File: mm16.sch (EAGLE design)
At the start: 58 parts, among them IC101 ATMEGA32-PU, IC102 DS1337, IC103 MAX483CPA, IC201 LTV847, IC202 LTV847, IC203 LTV847, IC204 LTV847, Q1 32,768kHz

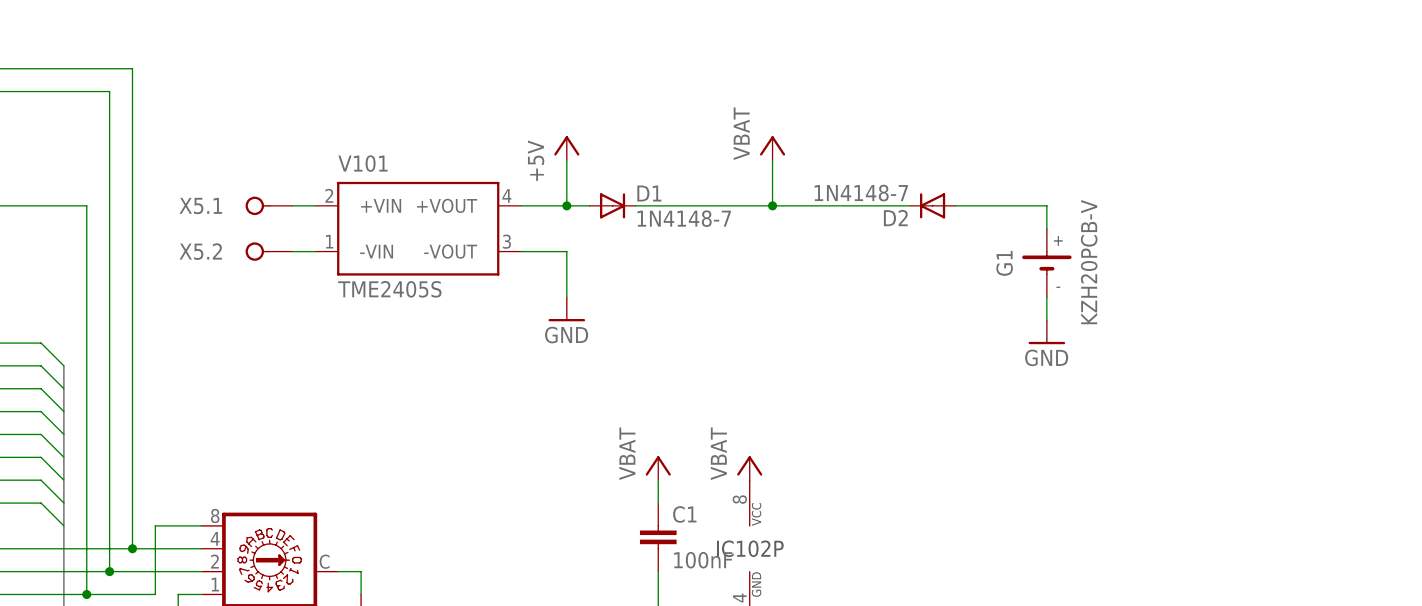
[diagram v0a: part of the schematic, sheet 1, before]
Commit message: Sicherheit und LED für Spannungsversorgung hinzugefuegt
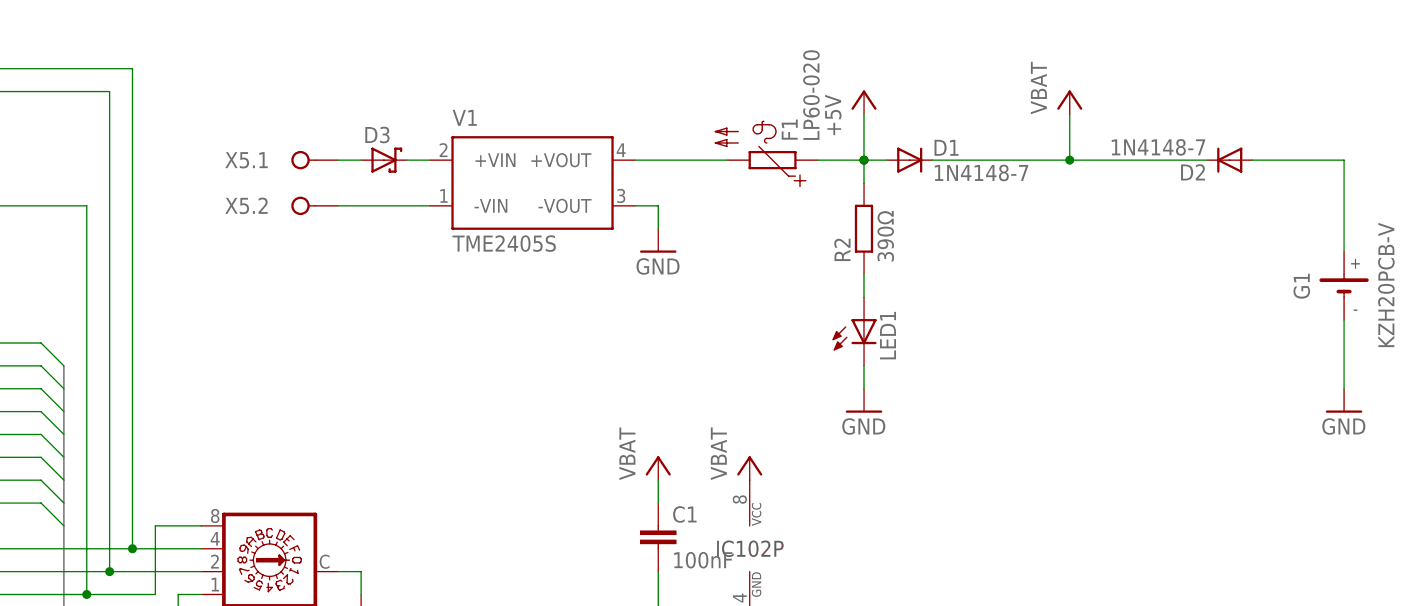
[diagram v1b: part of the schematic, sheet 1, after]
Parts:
- removed V101: TME2405S, schaltregler:TME2405S
- added D3: (no value), diode:SCHOTTKY-DIODEDO35-7
- added F1: LP60-020, sicherung:LP60-020
- added LED1: (no value), led:LED3MM
- added R2: 390Ω, passiv:R_0204/2V
- added V1: TME2405S, schaltregler:TME2405S
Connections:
- removed net N$17: V101.+VIN, X5.1.A
- removed net N$18: V101.-VIN, X5.2.A
- new net N$19: V1.-VIN, X5.2.A
- new net N$23: D3.C, V1.+VIN
- new net N$24: D3.A, X5.1.A
- new net N$41: F1.2, V1.+VOUT
- new net N$44: LED1.A, R2.1
- net +5V: now also F1.1, R2.2; no longer V101.+VOUT
- net GND: now also LED1.C, V1.-VOUT; no longer V101.-VOUT
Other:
- moved on the sheet: D1, D2, G1, X5.1, X5.2
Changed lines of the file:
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@@
 <?xml version="1.0" encoding="utf-8"?>
 <!DOCTYPE eagle SYSTEM "eagle.dtd">
-<eagle version="6.2">
+<eagle version="6.1">
 <drawing>
 <settings>
@@
 <part name="P+1" library="versorgung" deviceset="+5V" device=""/>
 <part name="IC103" library="ic-wandler" deviceset="MAX48*" device="CPA" technology="3"/>
-<part name="V101" library="schaltregler" deviceset="TME?*" device="24" technology="05S">
-<attribute name="MPN" value="TME 2405S"/>
-<attribute name="OC_FARNELL" value="1007547"/>
-<attribute name="OC_NEWARK" value="51R5329"/>
-</part>
-<part name="GND26" library="versorgung" deviceset="GND" device=""/>
 <part name="P+3" library="versorgung" deviceset="+5V" device=""/>
 <part name="C101" library="passiv" deviceset="C_" device="025-025X050" value="100nF"/>
@@
 <part name="R1" library="passiv" deviceset="R_" device="0204/2V" value="120Ω"/>
 <part name="G1" library="batterie" deviceset="KZH20" device="PCB-V"/>
+<part name="V1" library="schaltregler" deviceset="TME?*" device="24" technology="05S">
+<attribute name="MPN" value="TME 2405S"/>
+<attribute name="OC_FARNELL" value="1007547"/>
+<attribute name="OC_NEWARK" value="51R5329"/>
+</part>
+<part name="D3" library="diode" deviceset="SCHOTTKY-DIODE" device="DO35-7"/>
+<part name="LED1" library="led" deviceset="LED" device="3MM"/>
+<part name="R2" library="passiv" deviceset="R_" device="0204/2V" value="390Ω"/>
+<part name="F1" library="sicherung" deviceset="LP60" device="-020"/>
+<part name="GND40" library="versorgung" deviceset="GND" device=""/>
+<part name="GND41" library="versorgung" deviceset="GND" device=""/>
 </parts>
 <sheets>
@@
 <instance part="P+1" gate="1" x="50.8" y="172.72"/>
 <instance part="IC103" gate="G$1" x="137.16" y="15.24"/>
-<instance part="V101" gate="G$1" x="147.32" y="154.94"/>
-<instance part="GND26" gate="1" x="165.1" y="144.78"/>
-<instance part="P+3" gate="1" x="165.1" y="165.1"/>
+<instance part="P+3" gate="1" x="198.12" y="170.18"/>
 <instance part="C101" gate="G$1" x="40.64" y="109.22"/>
 <instance part="C102" gate="G$1" x="30.48" y="109.22"/>
@@
 <instance part="X1" gate="-15" x="182.88" y="48.26" rot="R180"/>
 <instance part="X1" gate="-16" x="182.88" y="45.72" rot="R180"/>
-<instance part="P+7" gate="VCC" x="187.96" y="165.1"/>
+<instance part="P+7" gate="VCC" x="220.98" y="170.18"/>
 <instance part="P+8" gate="VCC" x="185.42" y="129.54"/>
 <instance part="P+9" gate="VCC" x="175.26" y="129.54"/>
-<instance part="D1" gate="G$1" x="170.18" y="157.48"/>
-<instance part="D2" gate="G$1" x="205.74" y="157.48" rot="R180"/>
-<instance part="GND39" gate="1" x="218.44" y="142.24"/>
+<instance part="D1" gate="G$1" x="203.2" y="162.56"/>
+<instance part="D2" gate="G$1" x="238.76" y="162.56" rot="R180"/>
+<instance part="GND39" gate="1" x="251.46" y="134.62"/>
 <instance part="S1" gate="1" x="132.08" y="116.84" rot="R90"/>
 <instance part="P+2" gate="1" x="83.82" y="167.64"/>
-<instance part="X5" gate=".1" x="129.54" y="157.48"/>
-<instance part="X5" gate=".2" x="129.54" y="152.4"/>
+<instance part="X5" gate=".1" x="134.62" y="162.56"/>
+<instance part="X5" gate=".2" x="134.62" y="157.48"/>
 <instance part="X6" gate=".1" x="165.1" y="7.62" rot="R180"/>
 <instance part="X6" gate=".2" x="165.1" y="22.86" rot="R180"/>
 <instance part="R1" gate="G$1" x="157.48" y="15.24" rot="R90"/>
-<instance part="G1" gate="1" x="218.44" y="149.86"/>
+<instance part="G1" gate="1" x="251.46" y="147.32"/>
+<instance part="V1" gate="G$1" x="160.02" y="160.02"/>
+<instance part="D3" gate="G$1" x="144.78" y="162.56"/>
+<instance part="LED1" gate="G$1" x="198.12" y="144.78"/>
+<instance part="R2" gate="G$1" x="198.12" y="154.94" rot="R90"/>
+<instance part="F1" gate="G$1" x="187.96" y="162.56" rot="R90"/>
+<instance part="GND40" gate="1" x="175.26" y="152.4"/>
+<instance part="GND41" gate="1" x="198.12" y="134.62"/>
 </instances>
 <busses>
@@
 <pinref part="GND25" gate="1" pin="GND"/>
 <wire x1="83.82" y1="154.94" x2="83.82" y2="149.86" width="0.1524" layer="91"/>
-</segment>
-<segment>
-<pinref part="V101" gate="G$1" pin="-VOUT"/>
-<pinref part="GND26" gate="1" pin="GND"/>
-<wire x1="160.02" y1="152.4" x2="165.1" y2="152.4" width="0.1524" layer="91"/>
-<wire x1="165.1" y1="152.4" x2="165.1" y2="147.32" width="0.1524" layer="91"/>
 </segment>
 <segment>
@@
 <pinref part="GND39" gate="1" pin="GND"/>
 <pinref part="G1" gate="1" pin="-"/>
-<wire x1="218.44" y1="144.78" x2="218.44" y2="147.32" width="0.1524" layer="91"/>
+<wire x1="251.46" y1="137.16" x2="251.46" y2="144.78" width="0.1524" layer="91"/>
+</segment>
+<segment>
+<pinref part="LED1" gate="G$1" pin="C"/>
+<wire x1="198.12" y1="139.7" x2="198.12" y2="137.16" width="0.1524" layer="91"/>
+<pinref part="GND41" gate="1" pin="GND"/>
+</segment>
+<segment>
+<pinref part="V1" gate="G$1" pin="-VOUT"/>
+<wire x1="172.72" y1="157.48" x2="175.26" y2="157.48" width="0.1524" layer="91"/>
+<wire x1="175.26" y1="157.48" x2="175.26" y2="154.94" width="0.1524" layer="91"/>
+<pinref part="GND40" gate="1" pin="GND"/>
 </segment>
 </net>
@@
 <segment>
 <pinref part="P+3" gate="1" pin="+5V"/>
-<wire x1="165.1" y1="162.56" x2="165.1" y2="157.48" width="0.1524" layer="91"/>
-<pinref part="V101" gate="G$1" pin="+VOUT"/>
-<wire x1="165.1" y1="157.48" x2="160.02" y2="157.48" width="0.1524" layer="91"/>
+<wire x1="198.12" y1="167.64" x2="198.12" y2="162.56" width="0.1524" layer="91"/>
 <pinref part="D1" gate="G$1" pin="A"/>
-<wire x1="165.1" y1="157.48" x2="167.64" y2="157.48" width="0.1524" layer="91"/>
-<junction x="165.1" y="157.48"/>
+<wire x1="198.12" y1="162.56" x2="200.66" y2="162.56" width="0.1524" layer="91"/>
+<junction x="198.12" y="162.56"/>
+<pinref part="R2" gate="G$1" pin="2"/>
+<wire x1="198.12" y1="160.02" x2="198.12" y2="162.56" width="0.1524" layer="91"/>
+<junction x="198.12" y="162.56"/>
+<wire x1="198.12" y1="162.56" x2="193.04" y2="162.56" width="0.1524" layer="91"/>
+<pinref part="F1" gate="G$1" pin="1"/>
 </segment>
 <segment>
@@
 <pinref part="D1" gate="G$1" pin="C"/>
 <pinref part="P+7" gate="VCC" pin="VCC"/>
-<wire x1="172.72" y1="157.48" x2="187.96" y2="157.48" width="0.1524" layer="91"/>
-<wire x1="187.96" y1="157.48" x2="187.96" y2="162.56" width="0.1524" layer="91"/>
+<wire x1="205.74" y1="162.56" x2="220.98" y2="162.56" width="0.1524" layer="91"/>
+<wire x1="220.98" y1="162.56" x2="220.98" y2="167.64" width="0.1524" layer="91"/>
 <pinref part="D2" gate="G$1" pin="C"/>
-<wire x1="203.2" y1="157.48" x2="187.96" y2="157.48" width="0.1524" layer="91"/>
-<junction x="187.96" y="157.48"/>
+<wire x1="236.22" y1="162.56" x2="220.98" y2="162.56" width="0.1524" layer="91"/>
+<junction x="220.98" y="162.56"/>
 </segment>
 </net>
@@
 <segment>
 <pinref part="D2" gate="G$1" pin="A"/>
-<wire x1="208.28" y1="157.48" x2="218.44" y2="157.48" width="0.1524" layer="91"/>
-<wire x1="218.44" y1="157.48" x2="218.44" y2="154.94" width="0.1524" layer="91"/>
+<wire x1="241.3" y1="162.56" x2="251.46" y2="162.56" width="0.1524" layer="91"/>
+<wire x1="251.46" y1="162.56" x2="251.46" y2="152.4" width="0.1524" layer="91"/>
 <pinref part="G1" gate="1" pin="+"/>
 </segment>
@@
 <wire x1="165.1" y1="68.58" x2="167.64" y2="66.04" width="0.1524" layer="91"/>
 <label x="154.94" y="68.58" size="1.778" layer="95"/>
-</segment>
-</net>
-<net name="N$17" class="0">
-<segment>
-<pinref part="X5" gate=".1" pin="A"/>
-<pinref part="V101" gate="G$1" pin="+VIN"/>
-<wire x1="134.62" y1="157.48" x2="137.16" y2="157.48" width="0.1524" layer="91"/>
-</segment>
-</net>
-<net name="N$18" class="0">
-<segment>
-<pinref part="X5" gate=".2" pin="A"/>
-<pinref part="V101" gate="G$1" pin="-VIN"/>
-<wire x1="134.62" y1="152.4" x2="137.16" y2="152.4" width="0.1524" layer="91"/>
 </segment>
 </net>
@@
 </segment>
 </net>
+<net name="N$19" class="0">
+<segment>
+<pinref part="V1" gate="G$1" pin="-VIN"/>
+<wire x1="139.7" y1="157.48" x2="149.86" y2="157.48" width="0.1524" layer="91"/>
+<pinref part="X5" gate=".2" pin="A"/>
+</segment>
+</net>
+<net name="N$23" class="0">
+<segment>
+<pinref part="V1" gate="G$1" pin="+VIN"/>
+<pinref part="D3" gate="G$1" pin="C"/>
+<wire x1="147.32" y1="162.56" x2="149.86" y2="162.56" width="0.1524" layer="91"/>
+</segment>
+</net>
+<net name="N$24" class="0">
+<segment>
+<pinref part="D3" gate="G$1" pin="A"/>
+<wire x1="139.7" y1="162.56" x2="142.24" y2="162.56" width="0.1524" layer="91"/>
+<pinref part="X5" gate=".1" pin="A"/>
+</segment>
+</net>
+<net name="N$41" class="0">
+<segment>
+<pinref part="V1" gate="G$1" pin="+VOUT"/>
+<wire x1="182.88" y1="162.56" x2="172.72" y2="162.56" width="0.1524" layer="91"/>
+<pinref part="F1" gate="G$1" pin="2"/>
+</segment>
+</net>
+<net name="N$44" class="0">
+<segment>
+<pinref part="R2" gate="G$1" pin="1"/>
+<pinref part="LED1" gate="G$1" pin="A"/>
+<wire x1="198.12" y1="149.86" x2="198.12" y2="147.32" width="0.1524" layer="91"/>
+</segment>
+</net>
